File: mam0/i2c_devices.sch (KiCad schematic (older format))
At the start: 16 parts

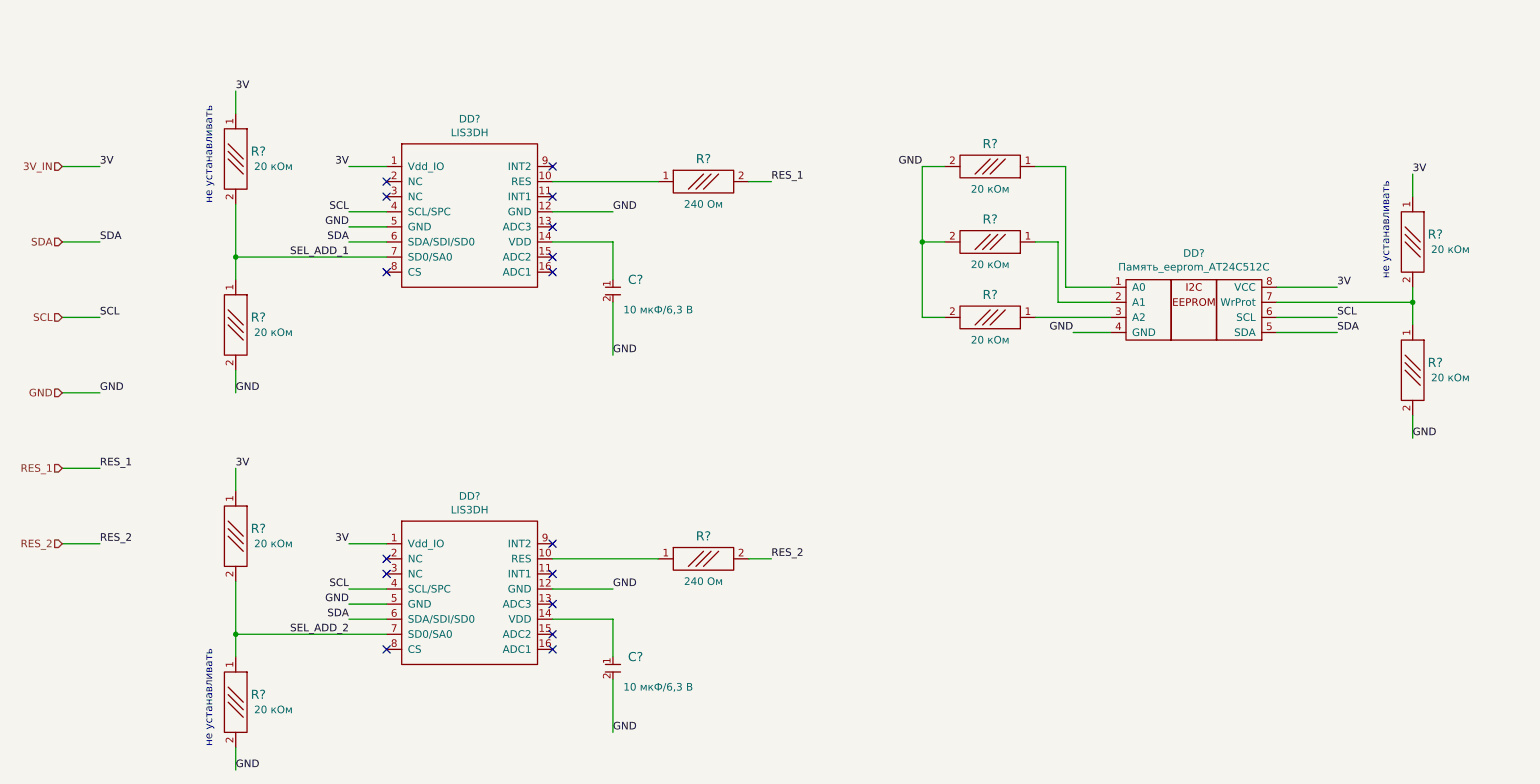
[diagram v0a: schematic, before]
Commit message: начата трассировка
сильно упрощенная схема
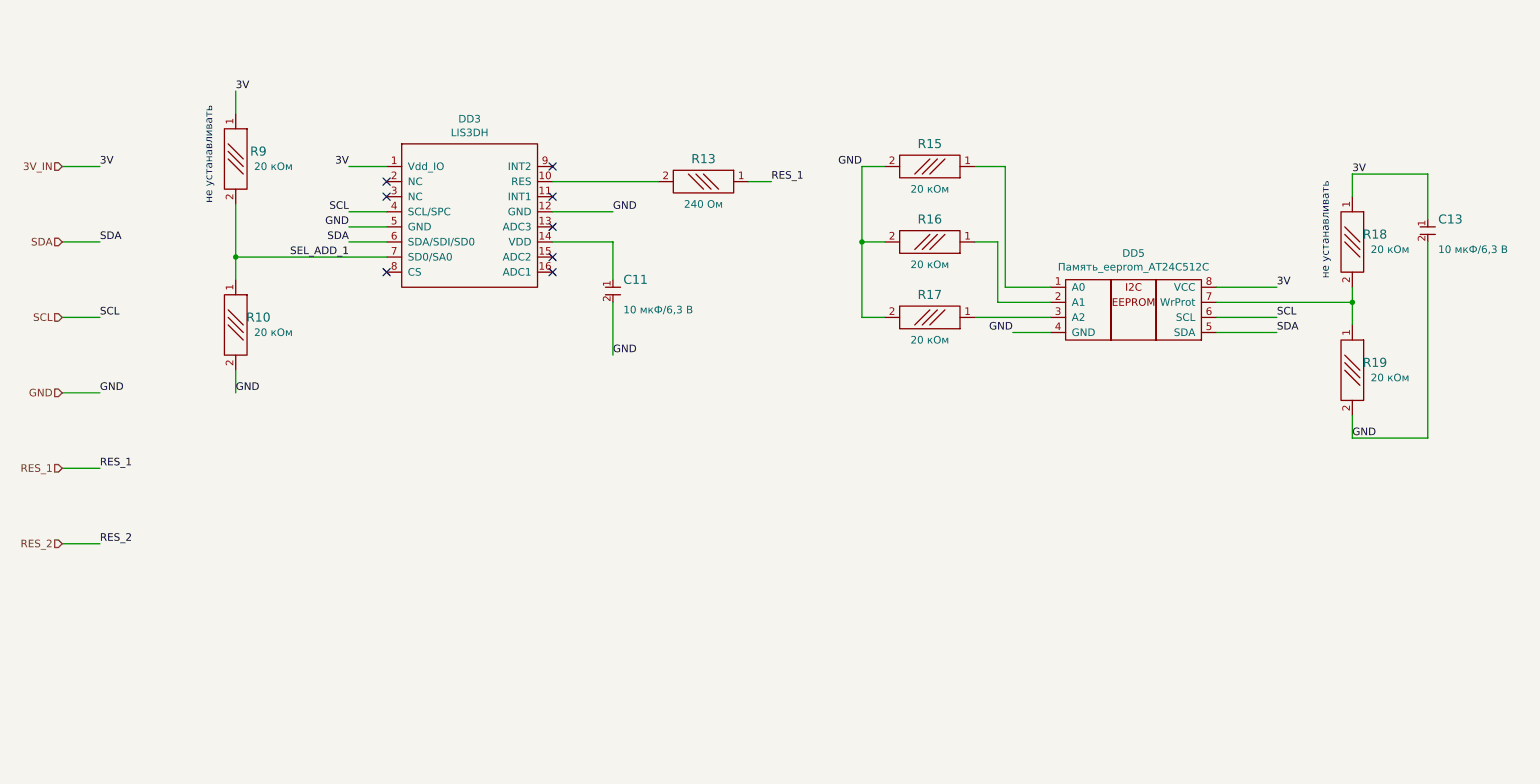
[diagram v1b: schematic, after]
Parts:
- removed C?: Конденсатор_керамический, N_RLC:Конденсатор_SMD_0603, symbol elements:Конденсатор_керамический
- removed DD?: LIS3DH, N_DD:акселерометр_LIS3DH, symbol elements:LIS3DH
- removed R? (x3): Резистор_0,065Вт, N_RLC:Резистор_SMD_0603_0,065_Вт, symbol elements:Резистор_0,065Вт
- added C13: Конденсатор_керамический, N_RLC:Конденсатор_SMD_0603, symbol elements:Конденсатор_керамический
- gave numbers to parts that had none: 11
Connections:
- net 3V_IN: now also C13.1
- net GND: now also C13.2
- net RES_1: now also R13.1; no longer R13.2
- net at DD3.10 (RES): now also R13.2; no longer R13.1
- no-connect marks 16 -> 8
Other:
- moved on the sheet: DD5, R15, R16, R17, R18, R19
